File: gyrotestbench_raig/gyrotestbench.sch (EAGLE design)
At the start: 80 parts, among them IC3 FT232RL, U1 TESTING_MPU-6050-1, U10 V_REG_LDOSMD, U2 TESTING_MPU-6050-1, U3 TESTING_MPU-6050-1, U8 TESTING_MPU-6050-1, U9 ATMEGA328P, X1 MINI-USB-UX60A-MB-5ST, Y1 8MHz

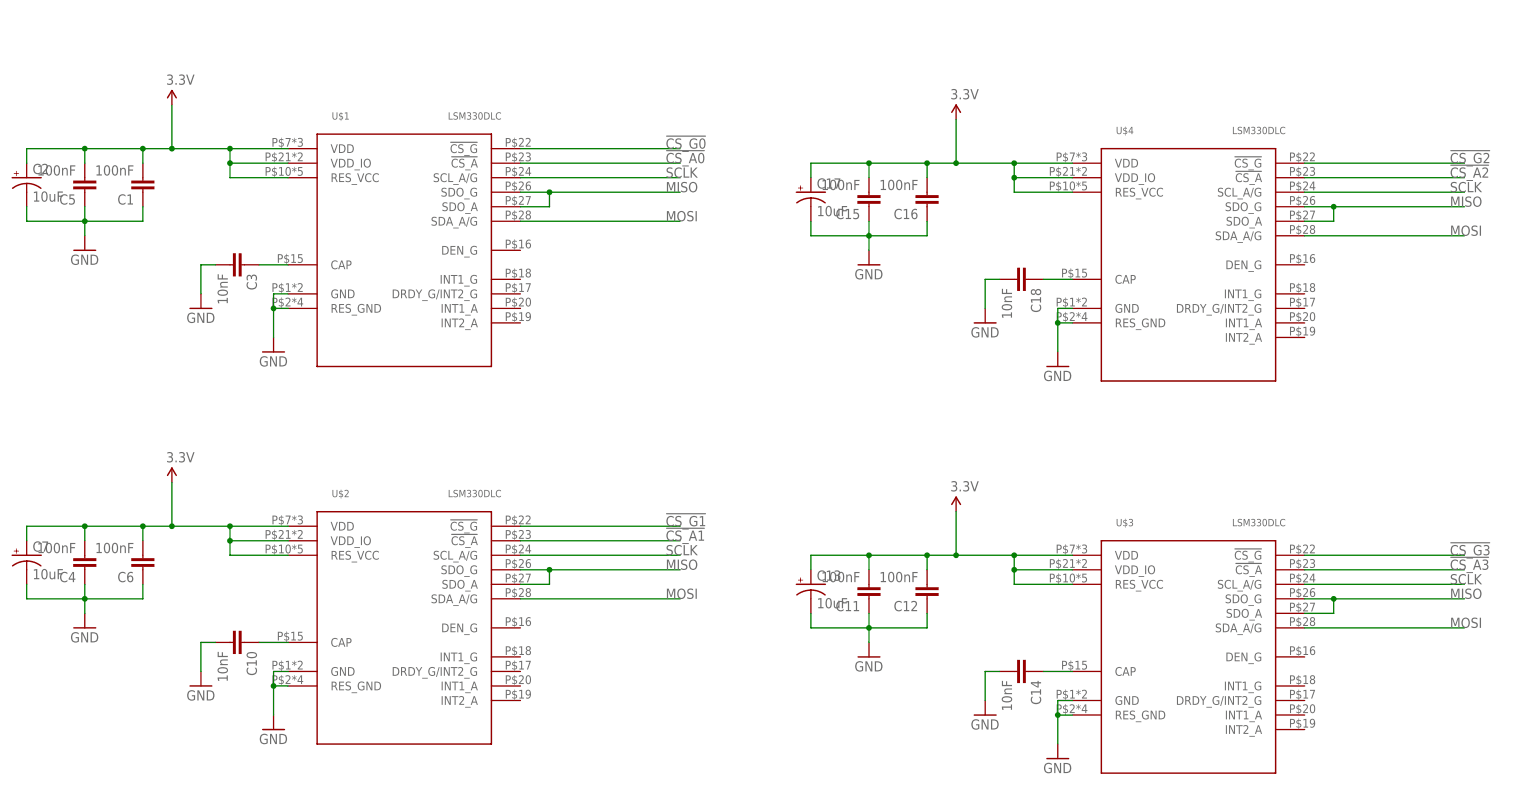
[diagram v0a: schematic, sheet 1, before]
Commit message: Severed RTS line on FTDI, added pull-ups to LSM chip select lines, and fixed silkscreen font
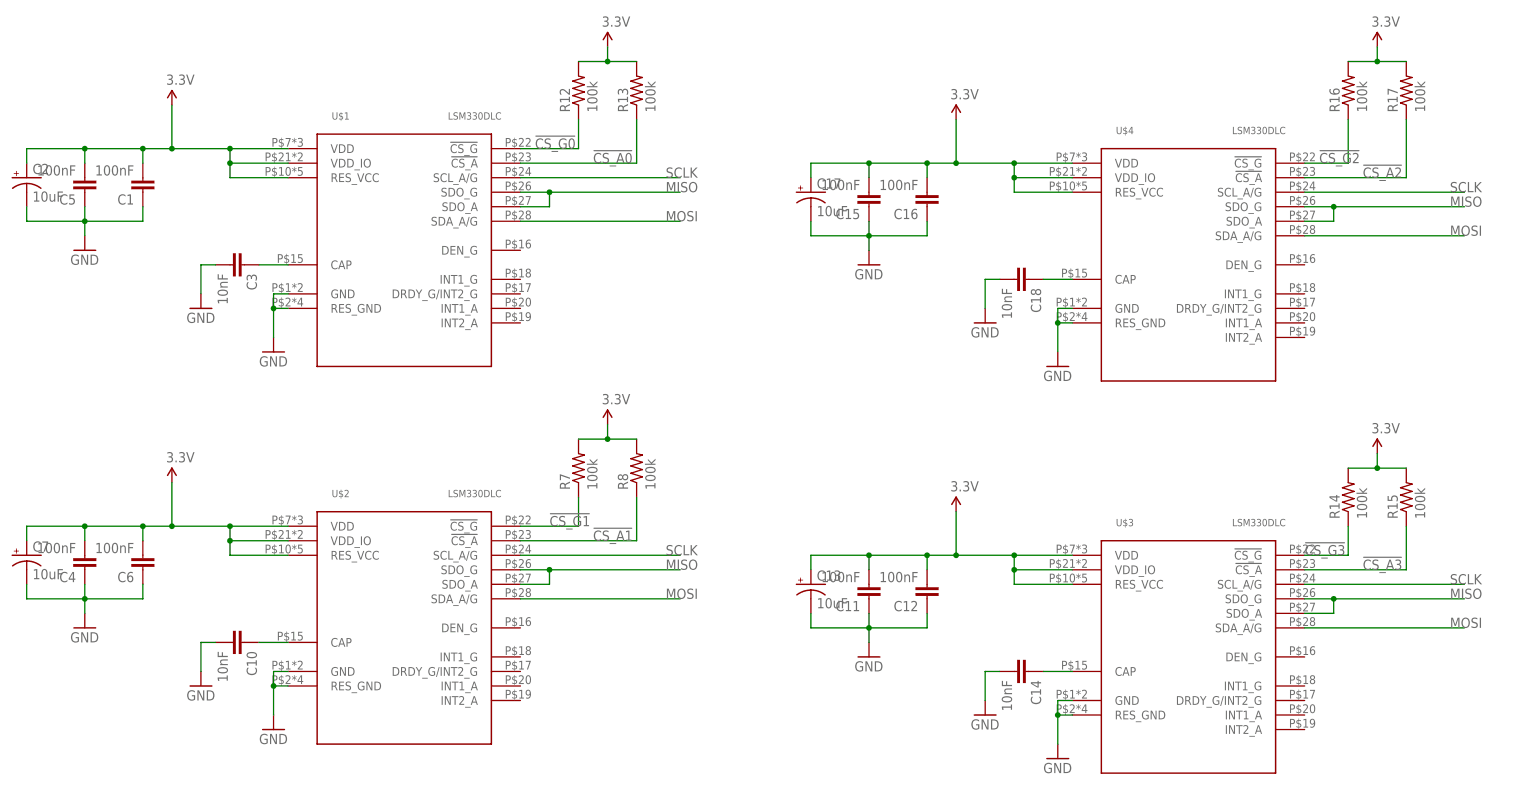
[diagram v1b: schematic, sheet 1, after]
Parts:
- added R12, R13, R14, R15, R16, R17, R7, R8: 100k, SparkFun-Resistors:RESISTOR0603-RES
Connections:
- net !CS_A0: now also R13.1
- net !CS_A1: now also R8.1
- net !CS_A2: now also R17.1
- net !CS_A3: now also R15.1
- net !CS_G0: now also R12.1
- net !CS_G1: now also R7.1
- net !CS_G2: now also R16.1
- net !CS_G3: now also R14.1
- net 3.3V: now also R12.2, R13.2, R14.2, R15.2, R16.2, R17.2, R7.2, R8.2
- net RESET: no longer IC3.!RTS
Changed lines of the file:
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@@
 <?xml version="1.0" encoding="utf-8"?>
 <!DOCTYPE eagle SYSTEM "eagle.dtd">
-<eagle version="6.2">
+<eagle version="6.4">
 <drawing>
 <settings>
@@
 </part>
 <part name="X1" library="con-hirose" deviceset="MINI-USB-" device="UX60A-MB-5ST"/>
+<part name="R7" library="SparkFun-Resistors" deviceset="RESISTOR" device="0603-RES" value="100k"/>
+<part name="R8" library="SparkFun-Resistors" deviceset="RESISTOR" device="0603-RES" value="100k"/>
+<part name="R12" library="SparkFun-Resistors" deviceset="RESISTOR" device="0603-RES" value="100k"/>
+<part name="R13" library="SparkFun-Resistors" deviceset="RESISTOR" device="0603-RES" value="100k"/>
+<part name="R14" library="SparkFun-Resistors" deviceset="RESISTOR" device="0603-RES" value="100k"/>
+<part name="R15" library="SparkFun-Resistors" deviceset="RESISTOR" device="0603-RES" value="100k"/>
+<part name="R16" library="SparkFun-Resistors" deviceset="RESISTOR" device="0603-RES" value="100k"/>
+<part name="R17" library="SparkFun-Resistors" deviceset="RESISTOR" device="0603-RES" value="100k"/>
+<part name="SUPPLY21" library="SparkFun-Aesthetics" deviceset="3.3V" device=""/>
+<part name="SUPPLY22" library="SparkFun-Aesthetics" deviceset="3.3V" device=""/>
+<part name="SUPPLY23" library="SparkFun-Aesthetics" deviceset="3.3V" device=""/>
+<part name="SUPPLY24" library="SparkFun-Aesthetics" deviceset="3.3V" device=""/>
 </parts>
 <sheets>
@@
 <instance part="C18" gate="G$1" x="76.2" y="5.08" rot="R270"/>
 <instance part="GND11" gate="1" x="71.12" y="-2.54"/>
+<instance part="R7" gate="G$1" x="0" y="-27.94" rot="R90"/>
+<instance part="R8" gate="G$1" x="10.16" y="-27.94" rot="R90"/>
+<instance part="R12" gate="G$1" x="0" y="38.1" rot="R90"/>
+<instance part="R13" gate="G$1" x="10.16" y="38.1" rot="R90"/>
+<instance part="R14" gate="G$1" x="134.62" y="-33.02" rot="R90"/>
+<instance part="R15" gate="G$1" x="144.78" y="-33.02" rot="R90"/>
+<instance part="R16" gate="G$1" x="134.62" y="38.1" rot="R90"/>
+<instance part="R17" gate="G$1" x="144.78" y="38.1" rot="R90"/>
+<instance part="SUPPLY21" gate="G$1" x="5.08" y="45.72"/>
+<instance part="SUPPLY22" gate="G$1" x="139.7" y="45.72"/>
+<instance part="SUPPLY23" gate="G$1" x="139.7" y="-25.4"/>
+<instance part="SUPPLY24" gate="G$1" x="5.08" y="-20.32"/>
 </instances>
 <busses>
@@
 <junction x="60.96" y="25.4"/>
 </segment>
+<segment>
+<pinref part="R7" gate="G$1" pin="2"/>
+<pinref part="R8" gate="G$1" pin="2"/>
+<wire x1="0" y1="-22.86" x2="5.08" y2="-22.86" width="0.1524" layer="91"/>
+<pinref part="SUPPLY24" gate="G$1" pin="3.3V"/>
+<wire x1="5.08" y1="-22.86" x2="10.16" y2="-22.86" width="0.1524" layer="91"/>
+<wire x1="5.08" y1="-22.86" x2="5.08" y2="-20.32" width="0.1524" layer="91"/>
+<junction x="5.08" y="-22.86"/>
+</segment>
+<segment>
+<pinref part="R12" gate="G$1" pin="2"/>
+<pinref part="R13" gate="G$1" pin="2"/>
+<wire x1="0" y1="43.18" x2="5.08" y2="43.18" width="0.1524" layer="91"/>
+<pinref part="SUPPLY21" gate="G$1" pin="3.3V"/>
+<wire x1="5.08" y1="43.18" x2="10.16" y2="43.18" width="0.1524" layer="91"/>
+<wire x1="5.08" y1="43.18" x2="5.08" y2="45.72" width="0.1524" layer="91"/>
+<junction x="5.08" y="43.18"/>
+</segment>
+<segment>
+<pinref part="R16" gate="G$1" pin="2"/>
+<pinref part="R17" gate="G$1" pin="2"/>
+<wire x1="134.62" y1="43.18" x2="139.7" y2="43.18" width="0.1524" layer="91"/>
+<pinref part="SUPPLY22" gate="G$1" pin="3.3V"/>
+<wire x1="139.7" y1="43.18" x2="144.78" y2="43.18" width="0.1524" layer="91"/>
+<wire x1="139.7" y1="43.18" x2="139.7" y2="45.72" width="0.1524" layer="91"/>
+<junction x="139.7" y="43.18"/>
+</segment>
+<segment>
+<pinref part="R14" gate="G$1" pin="2"/>
+<pinref part="R15" gate="G$1" pin="2"/>
+<wire x1="134.62" y1="-27.94" x2="139.7" y2="-27.94" width="0.1524" layer="91"/>
+<pinref part="SUPPLY23" gate="G$1" pin="3.3V"/>
+<wire x1="139.7" y1="-27.94" x2="144.78" y2="-27.94" width="0.1524" layer="91"/>
+<wire x1="139.7" y1="-27.94" x2="139.7" y2="-25.4" width="0.1524" layer="91"/>
+<junction x="139.7" y="-27.94"/>
+</segment>
 </net>
 <net name="GND" class="0">
@@
 <segment>
 <pinref part="U$4" gate="G$1" pin="!CS_G"/>
-<wire x1="127" y1="25.4" x2="154.94" y2="25.4" width="0.1524" layer="91"/>
-<label x="152.4" y="25.4" size="1.778" layer="95"/>
+<wire x1="127" y1="25.4" x2="134.62" y2="25.4" width="0.1524" layer="91"/>
+<label x="129.54" y="25.4" size="1.778" layer="95"/>
+<pinref part="R16" gate="G$1" pin="1"/>
+<wire x1="134.62" y1="25.4" x2="134.62" y2="33.02" width="0.1524" layer="91"/>
 </segment>
 </net>
@@
 <segment>
 <pinref part="U$4" gate="G$1" pin="!CS_A"/>
-<wire x1="127" y1="22.86" x2="154.94" y2="22.86" width="0.1524" layer="91"/>
-<label x="152.4" y="22.86" size="1.778" layer="95"/>
+<wire x1="127" y1="22.86" x2="144.78" y2="22.86" width="0.1524" layer="91"/>
+<label x="137.16" y="22.86" size="1.778" layer="95"/>
+<pinref part="R17" gate="G$1" pin="1"/>
+<wire x1="144.78" y1="22.86" x2="144.78" y2="33.02" width="0.1524" layer="91"/>
 </segment>
 </net>
@@
 <segment>
 <pinref part="U$1" gate="G$1" pin="!CS_G"/>
-<wire x1="-10.16" y1="27.94" x2="17.78" y2="27.94" width="0.1524" layer="91"/>
-<label x="15.24" y="27.94" size="1.778" layer="95"/>
+<wire x1="-10.16" y1="27.94" x2="0" y2="27.94" width="0.1524" layer="91"/>
+<label x="-7.62" y="27.94" size="1.778" layer="95"/>
+<pinref part="R12" gate="G$1" pin="1"/>
+<wire x1="0" y1="27.94" x2="0" y2="33.02" width="0.1524" layer="91"/>
 </segment>
 </net>
@@
 <segment>
 <pinref part="U$1" gate="G$1" pin="!CS_A"/>
-<wire x1="-10.16" y1="25.4" x2="17.78" y2="25.4" width="0.1524" layer="91"/>
-<label x="15.24" y="25.4" size="1.778" layer="95"/>
+<wire x1="-10.16" y1="25.4" x2="10.16" y2="25.4" width="0.1524" layer="91"/>
+<label x="2.54" y="25.4" size="1.778" layer="95"/>
+<pinref part="R13" gate="G$1" pin="1"/>
+<wire x1="10.16" y1="25.4" x2="10.16" y2="33.02" width="0.1524" layer="91"/>
 </segment>
 </net>
@@
 <segment>
 <pinref part="U$2" gate="G$1" pin="!CS_G"/>
-<wire x1="-10.16" y1="-38.1" x2="17.78" y2="-38.1" width="0.1524" layer="91"/>
-<label x="15.24" y="-38.1" size="1.778" layer="95"/>
+<wire x1="-10.16" y1="-38.1" x2="0" y2="-38.1" width="0.1524" layer="91"/>
+<label x="-5.08" y="-38.1" size="1.778" layer="95"/>
+<pinref part="R7" gate="G$1" pin="1"/>
+<wire x1="0" y1="-38.1" x2="0" y2="-33.02" width="0.1524" layer="91"/>
 </segment>
 </net>
@@
 <segment>
 <pinref part="U$2" gate="G$1" pin="!CS_A"/>
-<wire x1="-10.16" y1="-40.64" x2="17.78" y2="-40.64" width="0.1524" layer="91"/>
-<label x="15.24" y="-40.64" size="1.778" layer="95"/>
+<wire x1="-10.16" y1="-40.64" x2="10.16" y2="-40.64" width="0.1524" layer="91"/>
+<label x="2.54" y="-40.64" size="1.778" layer="95"/>
+<pinref part="R8" gate="G$1" pin="1"/>
+<wire x1="10.16" y1="-40.64" x2="10.16" y2="-33.02" width="0.1524" layer="91"/>
 </segment>
 </net>
@@
 <segment>
 <pinref part="U$3" gate="G$1" pin="!CS_G"/>
-<wire x1="127" y1="-43.18" x2="154.94" y2="-43.18" width="0.1524" layer="91"/>
-<label x="152.4" y="-43.18" size="1.778" layer="95"/>
+<wire x1="127" y1="-43.18" x2="134.62" y2="-43.18" width="0.1524" layer="91"/>
+<label x="127" y="-43.18" size="1.778" layer="95"/>
+<pinref part="R14" gate="G$1" pin="1"/>
+<wire x1="134.62" y1="-43.18" x2="134.62" y2="-38.1" width="0.1524" layer="91"/>
 </segment>
 </net>
@@
 <segment>
 <pinref part="U$3" gate="G$1" pin="!CS_A"/>
-<wire x1="127" y1="-45.72" x2="154.94" y2="-45.72" width="0.1524" layer="91"/>
-<label x="152.4" y="-45.72" size="1.778" layer="95"/>
+<wire x1="127" y1="-45.72" x2="144.78" y2="-45.72" width="0.1524" layer="91"/>
+<label x="137.16" y="-45.72" size="1.778" layer="95"/>
+<pinref part="R15" gate="G$1" pin="1"/>
+<wire x1="144.78" y1="-45.72" x2="144.78" y2="-38.1" width="0.1524" layer="91"/>
 </segment>
 </net>
@@
 </segment>
 <segment>
-<pinref part="IC3" gate="1" pin="!RTS"/>
-<wire x1="-116.84" y1="-2.54" x2="-83.82" y2="-2.54" width="0.1524" layer="91"/>
-<label x="-88.9" y="-2.54" size="1.778" layer="95"/>
-</segment>
-<segment>

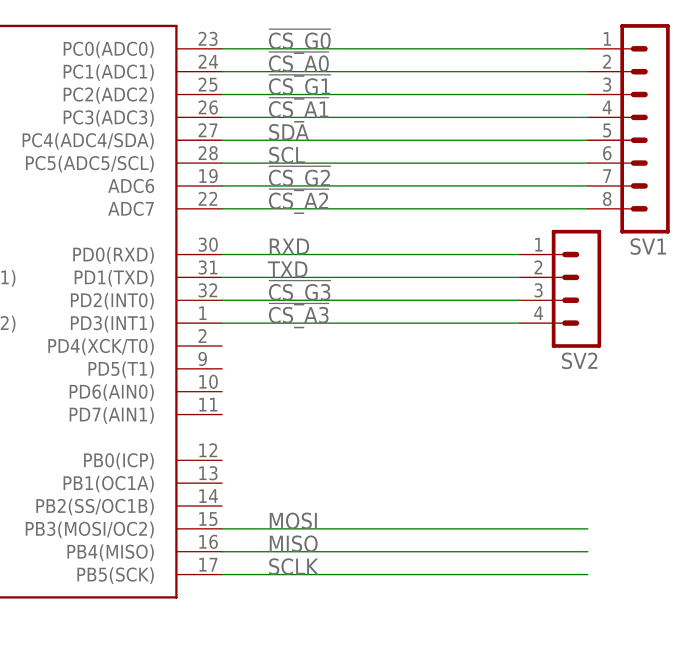
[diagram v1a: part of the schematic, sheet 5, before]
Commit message: Fixed interface problems, working on first stage IMU processing code
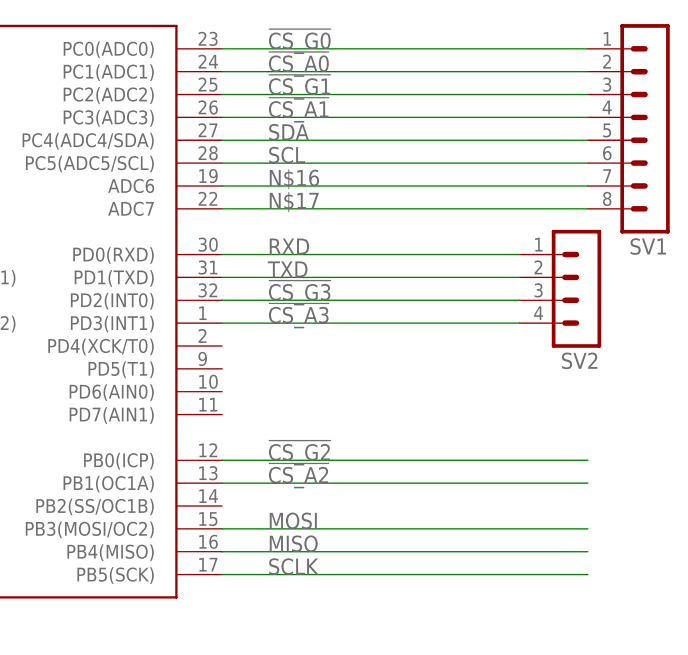
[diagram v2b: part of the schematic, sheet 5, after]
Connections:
- new net N$16: SV1.7, U9.ADC6
- new net N$17: SV1.8, U9.ADC7
- net !CS_A2: now also U9.PB1(OC1A); no longer SV1.8, U9.ADC7
- net !CS_G2: now also U9.PB0(ICP); no longer SV1.7, U9.ADC6
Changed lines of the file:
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@@
 <net name="!CS_G2" class="0">
 <segment>
-<pinref part="SV1" gate="1" pin="7"/>
-<pinref part="U9" gate="G$1" pin="ADC6"/>
-<wire x1="66.04" y1="10.16" x2="25.4" y2="10.16" width="0.1524" layer="91"/>
-<label x="30.48" y="10.16" size="1.778" layer="95"/>
+<pinref part="U9" gate="G$1" pin="PB0(ICP)"/>
+<wire x1="25.4" y1="-20.32" x2="66.04" y2="-20.32" width="0.1524" layer="91"/>
+<label x="30.48" y="-20.32" size="1.778" layer="95"/>
 </segment>
 </net>
 <net name="!CS_A2" class="0">
 <segment>
-<pinref part="U9" gate="G$1" pin="ADC7"/>
-<pinref part="SV1" gate="1" pin="8"/>
-<wire x1="25.4" y1="7.62" x2="66.04" y2="7.62" width="0.1524" layer="91"/>
-<label x="30.48" y="7.62" size="1.778" layer="95"/>
+<pinref part="U9" gate="G$1" pin="PB1(OC1A)"/>
+<wire x1="25.4" y1="-22.86" x2="66.04" y2="-22.86" width="0.1524" layer="91"/>
+<label x="30.48" y="-22.86" size="1.778" layer="95"/>
 </segment>
 </net>
@@
 </segment>
 </net>
+<net name="N$16" class="0">
+<segment>
+<pinref part="U9" gate="G$1" pin="ADC6"/>
+<pinref part="SV1" gate="1" pin="7"/>
+<wire x1="25.4" y1="10.16" x2="66.04" y2="10.16" width="0.1524" layer="91"/>
+<label x="30.48" y="10.16" size="1.778" layer="95"/>
+</segment>
+</net>
+<net name="N$17" class="0">
+<segment>
+<pinref part="U9" gate="G$1" pin="ADC7"/>
+<pinref part="SV1" gate="1" pin="8"/>
+<wire x1="25.4" y1="7.62" x2="66.04" y2="7.62" width="0.1524" layer="91"/>
+<label x="30.48" y="7.62" size="1.778" layer="95"/>
+</segment>
+</net>
